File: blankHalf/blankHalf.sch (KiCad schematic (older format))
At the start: 4 parts

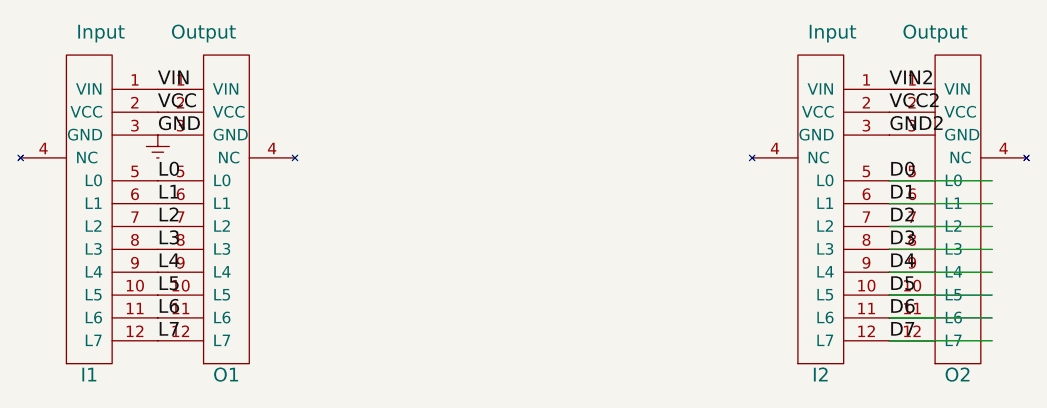
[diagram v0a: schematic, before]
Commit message: More work to ensure there are no errors from KiCAD's schematic checker. Fixed the multiplexer module, so that all 7 slaves will work (only 6 were working, due to a missing VCC to the "Next Output").
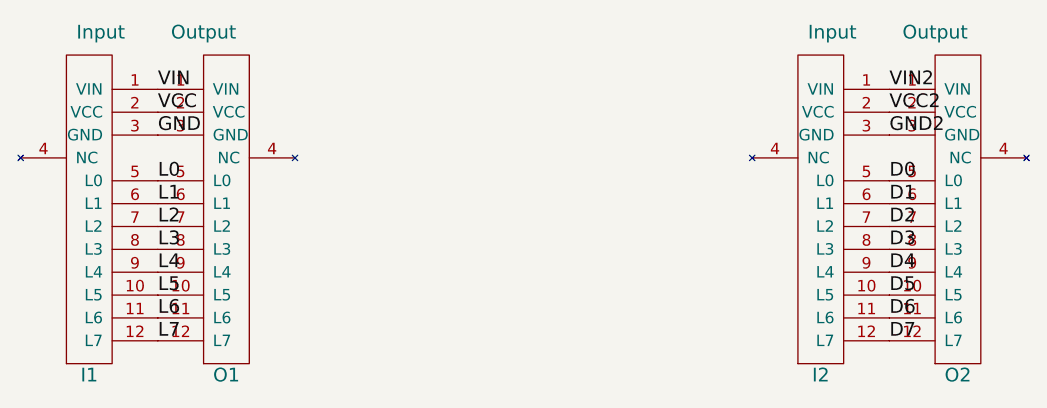
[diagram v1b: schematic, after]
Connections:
- net labels removed: Earth
- wire segments 8 -> 0
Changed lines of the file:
@@
 EESchema Schematic File Version 2
-LIBS:power
 LIBS:device
 LIBS:switches
@@
 LIBS:valves
 LIBS:eplay
-LIBS:blankHalf-cache
 EELAYER 25 0
 EELAYER END
@@
 Text Label 2400 2850 0    60   ~ 0
 L7
-$Comp
-L Earth #PWR01
-U 1 1 5AC24527
-P 2400 1950
-F 0 "#PWR01" H 2400 1700 50  0001 C CNN
-F 1 "Earth" H 2400 1800 50  0001 C CNN
-F 2 "" H 2400 1950 50  0001 C CNN
-F 3 "" H 2400 1950 50  0001 C CNN
-	1    2400 1950
-	1    0    0    -1
-$EndComp
 $Comp
 L Input I1
@@
 	1    0    0    -1
 $EndComp
-Wire Wire Line
-	6050 2850 5600 2850
-Wire Wire Line
-	5600 2750 6050 2750
-Wire Wire Line
-	6050 2650 5600 2650
-Wire Wire Line
-	5600 2550 6050 2550
-Wire Wire Line
-	6050 2450 5600 2450
-Wire Wire Line
-	5600 2350 6050 2350
-Wire Wire Line
-	6050 2250 5600 2250
-Wire Wire Line
-	5600 2150 6050 2150
 $EndSCHEMATC
